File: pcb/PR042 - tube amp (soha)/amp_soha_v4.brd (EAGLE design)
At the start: 81.1 x 45.8 mm, 56 parts, among them IC1 NE5532, IC2 7812, IC3 7912, Q1 J113, Q2 J113, Q3 J113, Q4 J113

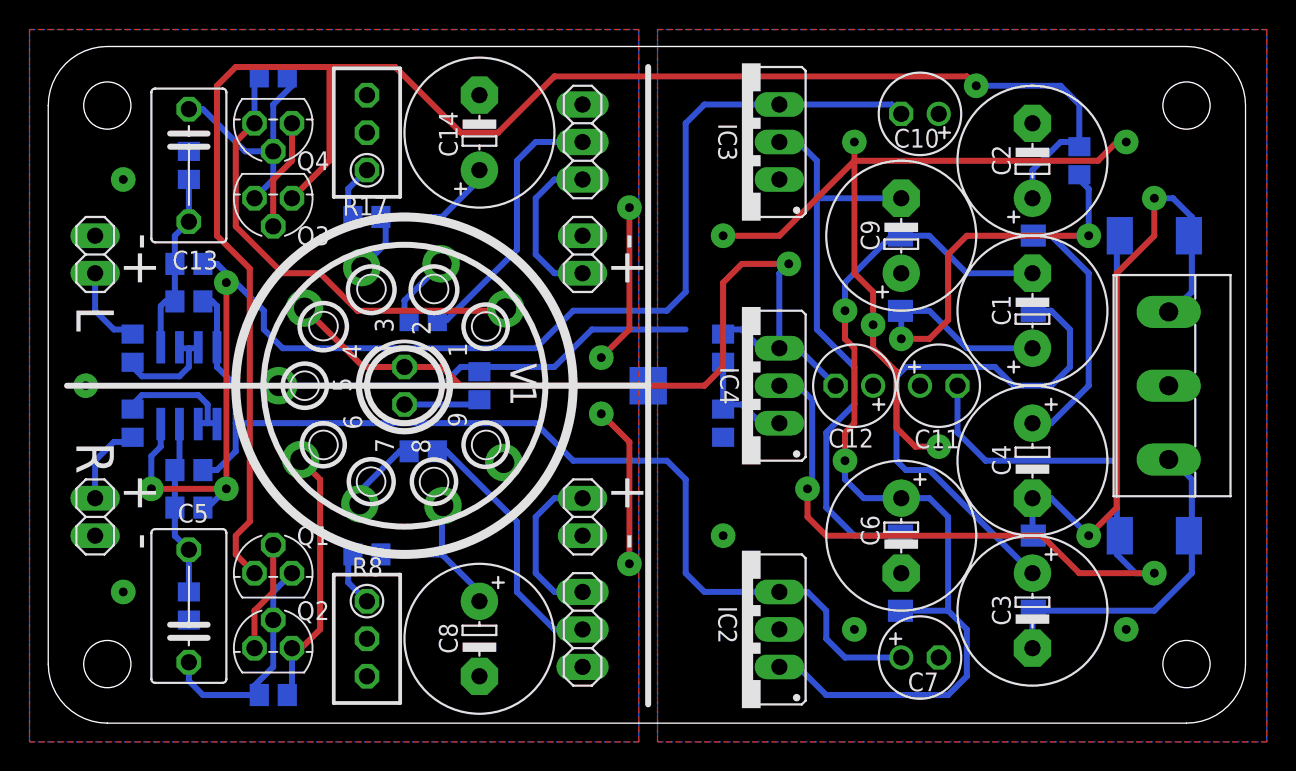
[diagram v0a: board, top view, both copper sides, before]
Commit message: 
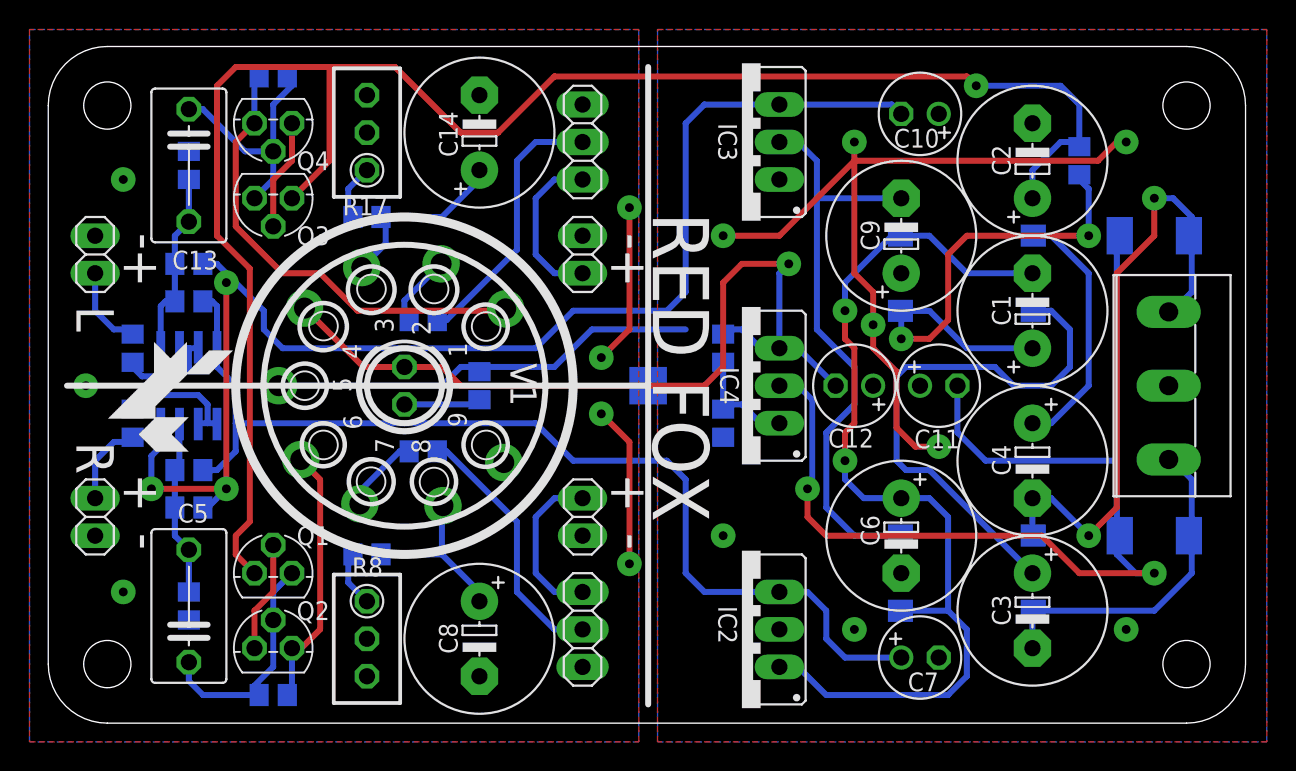
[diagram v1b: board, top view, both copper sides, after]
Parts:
- added U$1: (no value), amp_soha:FOX-2
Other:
- board text added: "RED FOX"
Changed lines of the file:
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@@
 <setting verticaltext="up"/>
 </settings>
-<grid distance="0.05" unitdist="inch" unit="inch" style="lines" multiple="1" display="yes" altdistance="0.0125" altunitdist="inch" altunit="inch"/>
+<grid distance="0.05" unitdist="inch" unit="mm" style="lines" multiple="1" display="yes" altdistance="0.0125" altunitdist="inch" altunit="inch"/>
 <layers>
 <layer number="1" name="Top" color="4" fill="1" visible="yes" active="yes"/>
@@
 <layer number="220" name="220bmp" color="21" fill="1" visible="no" active="no"/>
 <layer number="221" name="221bmp" color="22" fill="1" visible="no" active="no"/>
-<layer number="222" name="222bmp" color="23" fill="1" visible="no" active="no"/>
 <layer number="223" name="223bmp" color="24" fill="1" visible="no" active="no"/>
 <layer number="224" name="224bmp" color="25" fill="1" visible="no" active="no"/>
@@
 <wire x1="40.64" y1="22.86" x2="40.64" y2="1.27" width="0.4064" layer="22"/>
 <wire x1="40.64" y1="22.86" x2="40.64" y2="44.45" width="0.4064" layer="22"/>
+<text x="40.9575" y="34.6075" size="3.81" layer="21" font="vector" ratio="10" rot="SR270">RED FOX</text>
 </plain>
 <attributes>
@@
 </element>
 <element name="R6" library="amp_soha" package="SHORT" value="SHORT" x="40.64" y="22.86" rot="MR0"/>
+<element name="U$1" library="amp_soha" package="FOX-2" value="" x="3.81" y="26.67" rot="R270"/>
 </elements>
 <signals>
